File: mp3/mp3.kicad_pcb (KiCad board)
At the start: 2 copper layers, 21.9 x 52.1 mm, 33 parts, among them J1 USB4105-GF-A, J2 LEFT, J3 DEBUG, J4 RIGHT, U1 W25Q128JV, U2 RP2040, U3 MCP1702T-3302E_CB, Y1 12MHz

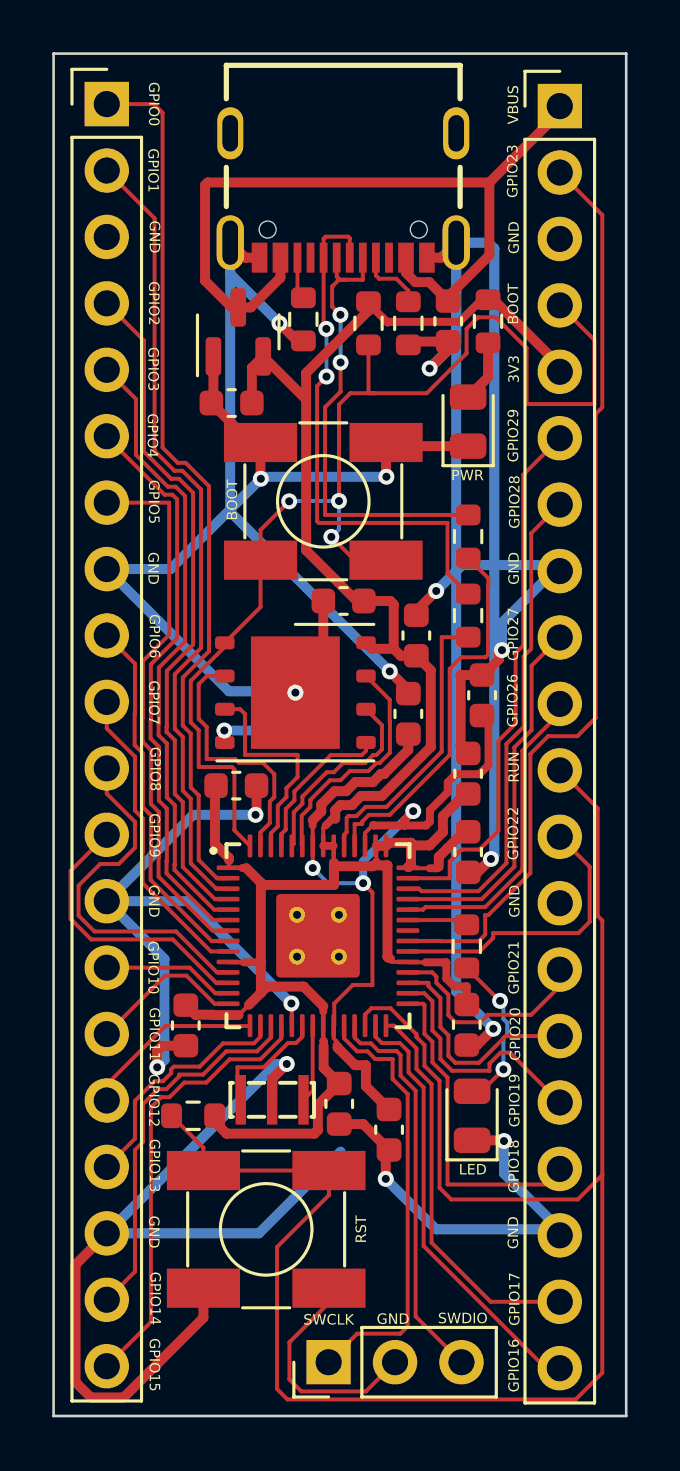
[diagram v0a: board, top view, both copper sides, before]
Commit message: added olin logo to pcb
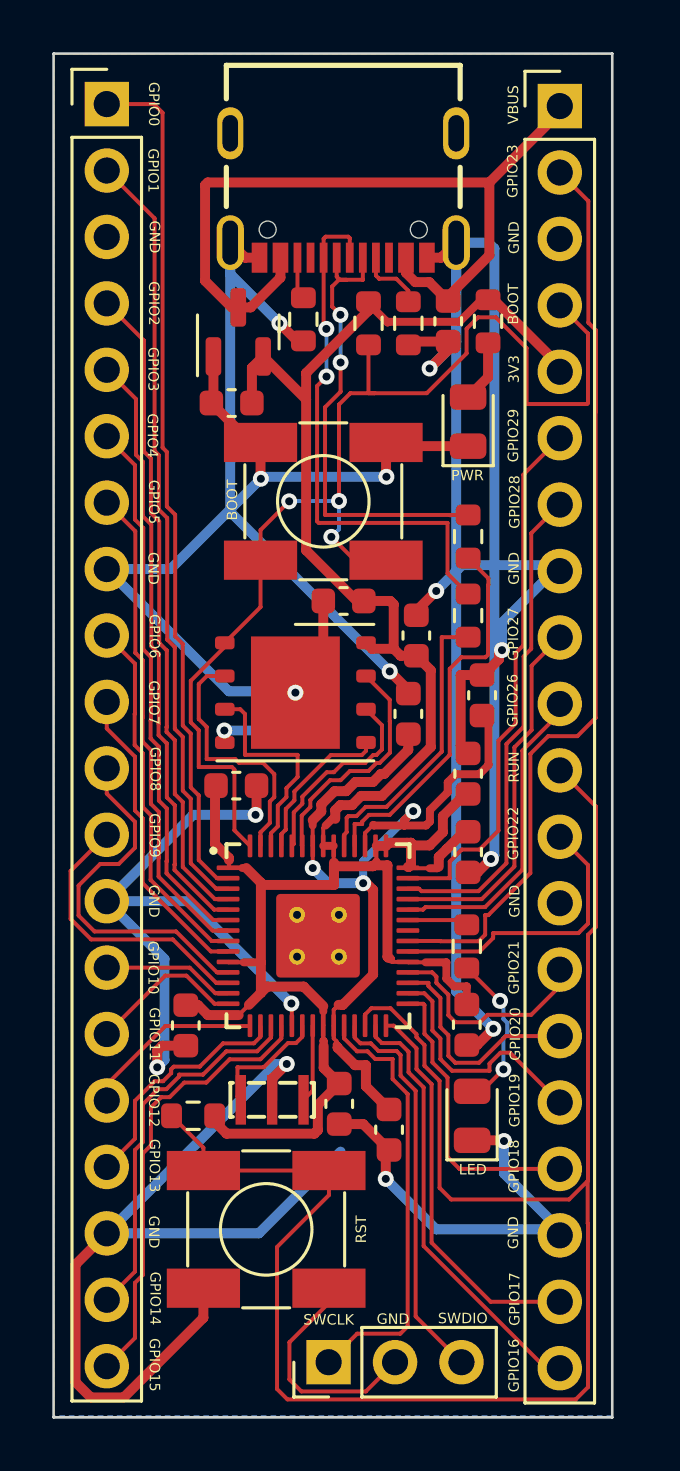
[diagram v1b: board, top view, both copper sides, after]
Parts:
- added OlinLogoTruncated_0.6in: G***, Eclectronics:OlinLogoTruncated_0.6in, B.Cu at (63.7, 102.0)
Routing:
- net /GPIO5: track 20.9 -> 18.7 mm
- net /GPIO18: track 12.4 -> 11.3 mm
- net /GPIO4: track 21.8 -> 20.8 mm
- net /GPIO2: track 26.0 -> 25.0 mm
- net /GPIO3: track 23.9 -> 22.9 mm
- net /GPIO1: track 30.7 -> 29.6 mm
- net /GPIO0: track 33.8 -> 32.8 mm
- net /RUN: track 69.2 -> 68.4 mm
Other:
- board size 21.9 x 52.1 mm -> 21.4 x 52.1 mm

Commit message: second revision of rp devboard
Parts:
- added OlinLogoTruncated_0.6in: G***, Eclectronics:OlinLogoTruncated_0.6in, B.Cu at (36.7, 80.8)
- moved BOOT 39.4 mm to (33.3, 76.9), turned to -90 degrees
- moved C10 39.3 mm to (37.7, 99.0)
- moved C3 39.2 mm to (30.9, 94.2), turned to 180 degrees
- moved LED 38.1 mm to (43.0, 98.1)
- moved C5 38.1 mm to (42.7, 94.7), turned to 0 degrees
- moved U1 38.0 mm to (34.0, 84.4)
- moved C4 37.8 mm to (36.0, 100.1)
- moved Y1 37.7 mm to (33.5, 100.0), turned to 90 degrees
- moved C11 37.7 mm to (38.3, 85.6)
- moved R7 37.4 mm to (42.6, 92.8), turned to 0 degrees
- moved C2 37.0 mm to (33.0, 88.1), turned to 180 degrees
- moved U2 37.0 mm to (36.8, 93.1)
- moved C6 36.6 mm to (42.5, 90.4), turned to 0 degrees
- moved C8 35.6 mm to (42.5, 88.9), turned to 0 degrees
- moved C1 35.5 mm to (38.0, 82.1), turned to -90 degrees
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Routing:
- net GND: track 236.5 -> 154.0 mm, vias 17 -> 16
- net +3V3: track 93.8 -> 72.3 mm
- net Net-(C10-Pad1): track 33.3 -> 23.9 mm
- net Net-(R5-Pad2): track 14.6 -> 6.27 mm
- net /BOOT: track 46.3 -> 39.0 mm, vias 3 -> 2
- net /SWDIO: track 15.2 -> 22.4 mm
- net /VBUS: track 31.0 -> 24.4 mm
- net /GPIO19: track 9.39 -> 15.5 mm
- net Net-(J1-PadB5): track 1.63 -> 7.61 mm
- net /SWCLK: track 16.7 -> 22.4 mm
- net /GPIO8: track 14.0 -> 8.39 mm
- net /GPIO22: track 11.2 -> 5.97 mm
- net /GPIO0: track 32.8 -> 27.6 mm
- net /GPIO14: track 14.5 -> 19.5 mm
- net /GPIO13: track 9.30 -> 14.3 mm
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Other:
- board size 21.4 x 52.1 mm -> 22.6 x 52.1 mm
